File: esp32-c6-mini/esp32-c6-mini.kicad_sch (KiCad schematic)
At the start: 1 part, among them U1 ESP32-C6-MINI-1-N4

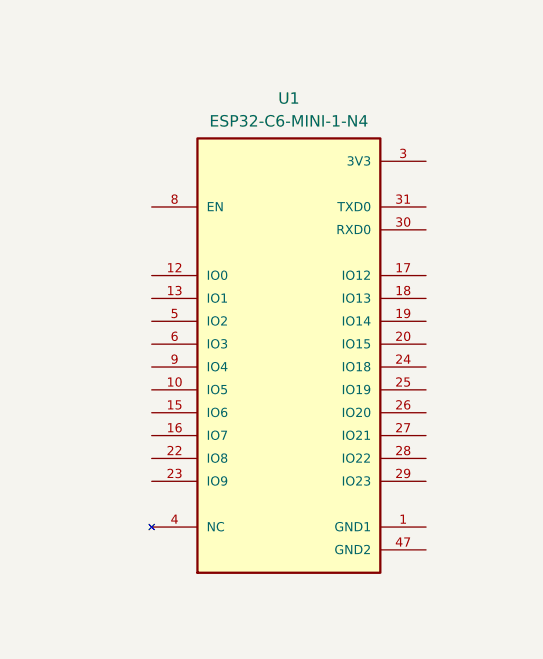
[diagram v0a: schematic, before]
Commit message: fix: use official espressif lib for esp32-c6 projects
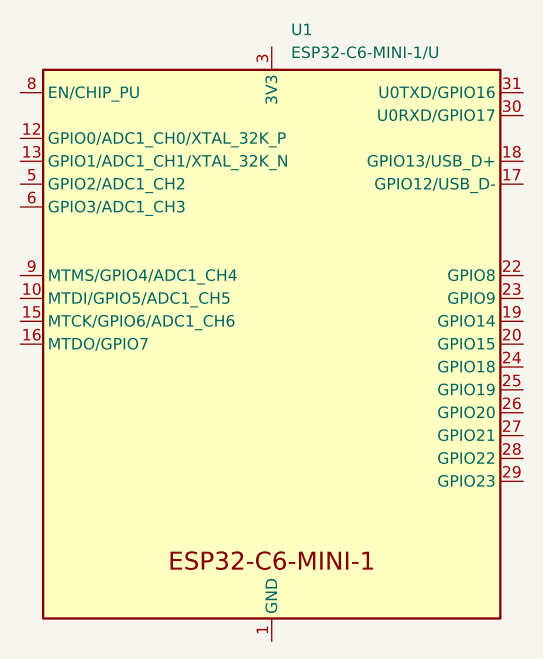
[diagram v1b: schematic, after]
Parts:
- removed U1: ESP32-C6-MINI-1-N4, ESP32:XCVR_ESP32-C6-MINI-1-N4, symbol ESP32:ESP32-C6-MINI-1-N4
- added U1: ESP32-C6-MINI-1/U, PCM_Espressif:ESP32-C6-MINI-1, symbol PCM_Espressif:ESP32-C6-MINI-1/U
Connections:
- new net: U1.1 (GND), U1.11 (GND), U1.14 (GND), U1.2 (GND), U1.36 (GND), U1.37 (GND), U1.38 (GND), U1.39 (GND), U1.40 (GND), U1.41 (GND), U1.42 (GND), U1.43 (GND), U1.44 (GND), U1.45 (GND), U1.46 (GND), U1.47 (GND), U1.48 (GND), U1.49 (GND), U1.50 (GND), U1.51 (GND), U1.52 (GND), U1.53 (GND)
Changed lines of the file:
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@@
 	(paper "A4")
 	(symbol
-		(lib_id "ESP32:ESP32-C6-MINI-1-N4")
-		(at 144.145 94.615 0)
+		(lib_id "PCM_Espressif:ESP32-C6-MINI-1/U")
+		(at 142.24 94.615 0)
 		(unit 1)
 		(exclude_from_sim no)
@@
 		(fields_autoplaced yes)
 		(property "Reference" "U1"
-			(at 144.145 67.31 0)
+			(at 144.3833 59.69 0)
 			(effects
 				(font
 					(size 1.27 1.27)
 				)
+				(justify left)
 			)
 		)
-		(property "Value" "ESP32-C6-MINI-1-N4"
-			(at 144.145 69.85 0)
+		(property "Value" "ESP32-C6-MINI-1/U"
+			(at 144.3833 62.23 0)
 			(effects
 				(font
 					(size 1.27 1.27)
 				)
+				(justify left)
 			)
 		)
-		(property "Footprint" "ESP32:XCVR_ESP32-C6-MINI-1-N4"
-			(at 144.145 94.615 0)
-			(effects
-				(font
-					(size 1.27 1.27)
-				)
-				(justify bottom)
-				(hide yes)
-			)
-		)
-		(property "Datasheet" ""
-			(at 144.145 94.615 0)
+		(property "Footprint" "PCM_Espressif:ESP32-C6-MINI-1"
+			(at 142.24 139.7 0)
 			(effects
 				(font
@@
 			)
 		)
-		(property "Description" ""
-			(at 144.145 94.615 0)
+		(property "Datasheet" "https://www.espressif.com/sites/default/files/documentation/esp32-c6-mini-1_datasheet_en.pdf"
+			(at 142.24 142.875 0)
 			(effects
 				(font
@@
 			)
 		)
-		(property "MF" "Espressif Systems"
-			(at 144.145 94.615 0)
+		(property "Description" "ESP32-C6-MINI-1 is a module that supports 2.4 GHz Wi-Fi 6 (802.11 ax), Bluetooth® 5 (LE), Zigbee and Thread (802.15.4)"
+			(at 142.24 94.615 0)
 			(effects
 				(font
 					(size 1.27 1.27)
 				)
-				(justify bottom)
 				(hide yes)
 			)
 		)
-		(property "MAXIMUM_PACKAGE_HEIGHT" "2.55 mm"
-			(at 144.145 94.615 0)
-			(effects
-				(font
-					(size 1.27 1.27)
-				)
-				(justify bottom)
-				(hide yes)
-			)
+		(pin "9"
 		)
-		(property "Package" "SMD-53 Espressif Systems"
-			(at 144.145 94.615 0)
-			(effects
-				(font
-					(size 1.27 1.27)
-				)
-				(justify bottom)
-				(hide yes)
-			)
+		(pin "4"
 		)
-		(property "Price" "None"
-			(at 144.145 94.615 0)
-			(effects
-				(font
-					(size 1.27 1.27)
-				)
-				(justify bottom)
-				(hide yes)
-			)
+		(pin "7"
 		)
-		(property "Check_prices" "https://www.snapeda.com/parts/ESP32-C6-MINI-1-N4/Espressif+Systems/view-part/?ref=eda"
-			(at 144.145 94.615 0)
-			(effects
-				(font
-					(size 1.27 1.27)
-				)
-				(justify bottom)
-				(hide yes)
-			)
+		(pin "32"
 		)
-		(property "STANDARD" "Manufacturer recommendations"
-			(at 144.145 94.615 0)
-			(effects
-				(font
-					(size 1.27 1.27)
-				)
-				(justify bottom)
-				(hide yes)
-			)
+		(pin "21"
 		)
-		(property "PARTREV" "1.0"
-			(at 144.145 94.615 0)
-			(effects
-				(font
-					(size 1.27 1.27)
-				)
-				(justify bottom)
-				(hide yes)
-			)
+		(pin "6"
 		)
-		(property "SnapEDA_Link" "https://www.snapeda.com/parts/ESP32-C6-MINI-1-N4/Espressif+Systems/view-part/?ref=snap"
-			(at 144.145 94.615 0)
-			(effects
-				(font
-					(size 1.27 1.27)
-				)
-				(justify bottom)
-				(hide yes)
-			)
+		(pin "33"
 		)
-		(property "MP" "ESP32-C6-MINI-1-N4"
-			(at 144.145 94.615 0)
-			(effects
-				(font
-					(size 1.27 1.27)
-				)
-				(justify bottom)
-				(hide yes)
-			)
+		(pin "10"
 		)
-		(property "Purchase-URL" "https://www.snapeda.com/api/url_track_click_mouser/?unipart_id=12774151&manufacturer=Espressif Systems&part_name=ESP32-C6-MINI-1-N4&search_term=esp32-c6-mini"
-			(at 144.145 94.615 0)
-			(effects
-				(font
-					(size 1.27 1.27)
-				)
-				(justify bottom)
-				(hide yes)
-			)
+		(pin "15"
 		)
-		(property "Description_1" "802.15.4, Bluetooth, WiFi 802.11ax, Bluetooth v5.0, Zigbee® Transceiver Module 2.4GHz Antenna Not Included Surface Mount"
-			(at 144.145 94.615 0)
-			(effects
-				(font
-					(size 1.27 1.27)
-				)
-				(justify bottom)
-				(hide yes)
-			)
+		(pin "5"
 		)
-		(property "Availability" "In Stock"
-			(at 144.145 94.615 0)
-			(effects
-				(font
-					(size 1.27 1.27)
-				)
-				(justify bottom)
-				(hide yes)
-			)
+		(pin "34"
 		)
-		(property "MANUFACTURER" "Espressif Systems"
-			(at 144.145 94.615 0)
-			(effects
-				(font
-					(size 1.27 1.27)
-				)
-				(justify bottom)
-				(hide yes)
-			)
+		(pin "12"
+		)
+		(pin "13"
+		)
+		(pin "35"
+		)
+		(pin "8"
+		)
+		(pin "16"
+		)
+		(pin "53"
+		)
+		(pin "52"
+		)
+		(pin "51"
+		)
+		(pin "48"
+		)
+		(pin "30"
+		)
+		(pin "50"
+		)
+		(pin "18"
 		)
 		(pin "31"
 		)
+		(pin "49"
+		)
+		(pin "2"
+		)
+		(pin "37"
+		)
+		(pin "40"
+		)
+		(pin "42"
+		)
+		(pin "14"
+		)
+		(pin "38"
+		)
+		(pin "43"
+		)
+		(pin "3"
+		)
+		(pin "1"
+		)
+		(pin "11"
+		)
+		(pin "36"
+		)
+		(pin "39"
+		)
+		(pin "41"
+		)
+		(pin "44"
+		)
+		(pin "45"
+		)
+		(pin "46"
+		)
+		(pin "47"
+		)
+		(pin "23"
+		)
+		(pin "20"
+		)
+		(pin "25"
+		)
+		(pin "17"
+		)
 		(pin "22"
 		)
-		(pin "21"
-		)
-		(pin "12"
-		)
-		(pin "23"
+		(pin "19"
 		)
 		(pin "24"
@@
 		(pin "26"
 		)
-		(pin "15"
-		)
-		(pin "6"
-		)
-		(pin "32"
-		)
-		(pin "13"
-		)
-		(pin "10"
-		)
-		(pin "34"
-		)
-		(pin "5"
-		)
-		(pin "35"
-		)
-		(pin "33"
-		)
-		(pin "9"
-		)
-		(pin "4"
-		)
-		(pin "16"
-		)
-		(pin "7"
-		)
-		(pin "8"
-		)
-		(pin "3"
-		)
-		(pin "30"
-		)
-		(pin "17"
-		)
-		(pin "18"
-		)
-		(pin "19"
-		)
-		(pin "20"
-		)
-		(pin "25"
-		)
-		(pin "49_4"
-		)
-		(pin "46"
-		)
-		(pin "2"
+		(pin "27"
 		)
 		(pin "29"
 		)
-		(pin "48"
-		)
-		(pin "49_8"
-		)
-		(pin "41"
-		)
-		(pin "40"
-		)
-		(pin "27"
-		)
 		(pin "28"
 		)
-		(pin "39"
-		)
-		(pin "43"
-		)
-		(pin "11"
-		)
-		(pin "37"
-		)
-		(pin "36"
-		)
-		(pin "42"
-		)
-		(pin "38"
-		)
-		(pin "44"
-		)
-		(pin "47"
-		)
-		(pin "49_1"
-		)
-		(pin "49_2"
-		)
-		(pin "1"
-		)
-		(pin "14"
-		)
-		(pin "45"
-		)
-		(pin "49_3"
-		)
-		(pin "49_5"
-		)
-		(pin "49_6"
-		)
-		(pin "49_7"
-		)
-		(pin "49_9"
-		)
-		(pin "50"
-		)
-		(pin "51"
-		)
-		(pin "52"
-		)
-		(pin "53"
-		)
 		(instances
